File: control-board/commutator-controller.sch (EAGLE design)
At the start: 40 parts, among them U1 IS31FL3193, U2 LTC4425EMSE#PBF, U3 TEENSY_LC, U4 PTN04050C, U5 TMC2130

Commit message: Nearly complete control board
- Silkscreen still needs work: button labels, device label, etc
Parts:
- removed 1.2M, 1.5M: (no value), jonnew:R_0603
- removed IREF_AIN: (no value), jonnew:TP_2MM
- removed J2: (no value), jonnew:PINHD-1X4
- removed R17: 10k, jonnew:R_0402
- removed S4: (no value), jonnew:TOUCH_2X2CM
- removed TP1: RESET, jonnew:TP_1MM
- added GND1, GND2: (no value), jonnew:TPB2,54
- added J1: (no value), jonnew:PINHD-1X4_SMD-0.1"
- added R11: 500, jonnew:R_0603
- added R12, R13: 4.7k, jonnew:R_0603
- +3.3V, +5V, +5V1, GND: device jonnew:TP_2MM -> jonnew:TPB2,54
- C10: value 22uF -> 1F; device jonnew:C_1206 -> jonnew:C-POL_1210
- C2: value 10nF -> 22uF; device jonnew:C_0402 -> jonnew:C_1206
- C3: value 1uF/50V -> 22uF; device jonnew:C_0603 -> jonnew:C_1206
- C5: value 1F -> 100 uF; device jonnew:C-POL_1210 -> jonnew:C-POL_0807
- C6: value 2.2uF -> 100uF; device jonnew:C_0805 -> jonnew:C-POL_0807
- C7: value 100uF -> 2.2uF; device jonnew:C-POL_0807 -> jonnew:C_0805
- C8: value 100 uF -> 10nF; device jonnew:C-POL_0807 -> jonnew:C_0402
- C9: value 22uF -> 1uF; device jonnew:C_1206 -> jonnew:C_0603
- R1: device jonnew:R_0402 -> jonnew:R_0603
- R10, R9: value 4.7k -> 10k; device jonnew:R_0402 -> jonnew:R_0603
- R2: value 10k -> 1.5M
- R3: value 10k -> 1.33k
- R4: value 0 -> 1.2M
- R5: value DNP -> 0
- R6: value 10k -> DNP
- R7: value 1.33k -> 10k
- R8: value 500 -> 10k
- S1, S2: device jonnew:SPST_TACT_EVQP7 -> jonnew:TOUCH_2X2CM
- S3: device jonnew:TOUCH_2X2CM -> jonnew:SPST_TACT_EVQP7
- U1: value IS31FL3193 -> PTN04050C; device jonnew:IS31FL3193 -> jonnew:VREG_ADJ_R-PDSS-B4
- U3: value TEENSY_LC -> IS31FL3193; device jonnew:TEENSY_LC_SMD -> jonnew:IS31FL3193
- U4: value PTN04050C -> TMC2130; device jonnew:VREG_ADJ_R-PDSS-B4 -> jonnew:SILENT-STEPPER-STICK-TMC2130_SMD
- U5: value TMC2130 -> TEENSY_LC; device jonnew:SILENT-STEPPER-STICK-TMC2130_SMD -> jonnew:TEENSY_LC_SMD
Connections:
- removed net IREF: IREF_AIN.TP
- removed net N$23: S2.P, S2.P1, TP1.TP
- new net CFG-3/!TMC_CS: U4.CS/CFG3, U5.15/A1/T
- new net DIR: U4.DIR, U5.14/A0
- new net STEP: U4.STEP, U5.16/A2/T/PWM
- new net TMC_EN: U4.EN/CFG6, U5.17/A3/T/PWM
- net !IS31_SHDN: now also R8.1, U3.!SHDN, U5.2; no longer R17.1, U1.!SHDN
- net !PFO: now also R7.1, U5.23/A9/SDA1/T/PWM; no longer R6.1, U3.2
- net +3V3: now also R1.2, R12.1, R13.1, R7.2, U4.VIO, U5.3.3V0; no longer R6.2, U3.3.3V0
- net +5V0: now also C2.1, C5.+, R5.2, U1.VI; no longer C8.+, C9.1, R10.1, R4.2, R9.1, U4.VI
- net CCW: now also S2.1, U5.4/PWM; no longer S4.1, U3.1/TX1/T
- net CFG-0/MISO: now also U4.MISO/GFG0, U5.12/MISO; no longer U3.12/MISO
- net CFG-1/MOSI: now also U4.MOSI/GFG1, U5.11/MOSI; no longer U3.11/MOSI
- net CFG-2/SCLK: now also U4.SCLK/CFG2, U5.13/SCK0/LED; no longer U3.13/SCK0/LED
- net CHRG_CURR: now also R11.2, U5.21/A7; no longer R8.2
- net CW: now also S1.1, U5.0/RX1/T; no longer S3.1, U3.0/RX1/T
- net GND: now also C10.-, C6.-, C7.2, C8.2, GND1.TP, GND2.TP, R10.1, R11.1, R6.1, R8.2, R9.1, S3.S, S3.S1, U3.AD; no longer C10.2, C6.2, C7.-, C8.-, R17.2, R2.1, R5.1, R7.1, R8.1, S1.S1, S2.S, S2.S1, U1.AD
- net MOT_POW_EN: now also R10.2, U5.22/A8/SCL1/T/PWM; no longer R3.2, U3.3/PWM
- net N$1: now also R4.1; no longer 1.2M.1
- net N$10: now also U3.OUT2; no longer U1.OUT2
- net N$14: now also C10.+; no longer C5.+
- net N$2: now also R2.1, R4.2; no longer 1.2M.2, 1.5M.1
- net N$3: now also U3.OUT1; no longer U1.OUT1
- net N$4: now also R5.1, R6.2; no longer R4.1, R5.2
- net N$45: now also U3.OUT3; no longer U1.OUT3
- net N$5: now also J1.1, U4.M1B; no longer J2.1, U5.M1B
- net N$6: now also J1.2, U4.M1A; no longer J2.2, U5.M1A
- net N$7: now also J1.3, U4.M2A; no longer J2.3, U5.M2A
- net N$8: now also J1.4, U4.M2B; no longer J2.4, U5.M2B
- net N$9: now also R3.2, U1.ADJ; no longer R7.2, U4.ADJ
- net PROGRAM: now also S3.P, S3.P1, U5.PROGRAM; no longer S1.P, S1.P1, U3.PROGRAM
- net SCL: now also R13.2, U3.SCL, U5.19/A5/SCL0/T; no longer R10.2, U1.SCL, U3.19/A5/SCL0/T
- net SDA: now also R12.2, U3.SDA, U5.18/A4/SDA0/T; no longer R9.2, U1.SDA, U3.18/A4/SDA0/T
- net VCC: now also C7.1, C8.1, C9.1, R2.2, U3.VCC, U5.VIN; no longer 1.5M.2, C2.1, C3.1, C6.1, R1.2, U1.VCC, U3.VIN, U5.VIO
- net VMID_SEL: now also R9.2, U5.20/A6/SCK1/PWM; no longer R2.2, U3.4/PWM
- net VMOT: now also C3.1, C6.+, U1.VO, U4.VM; no longer C10.1, C7.+, U4.VO, U5.VM
- net V_BM: now also U3.V_BM, U5.3/PWM; no longer U1.V_BM
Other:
- note removed: "Teensy reset (jumper wire to reset pad on Teensy)"
- moved on the sheet: +3.3V, +5V, +5V1, C10, C2, C3, C5, C6, C7, C8, C9, GND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

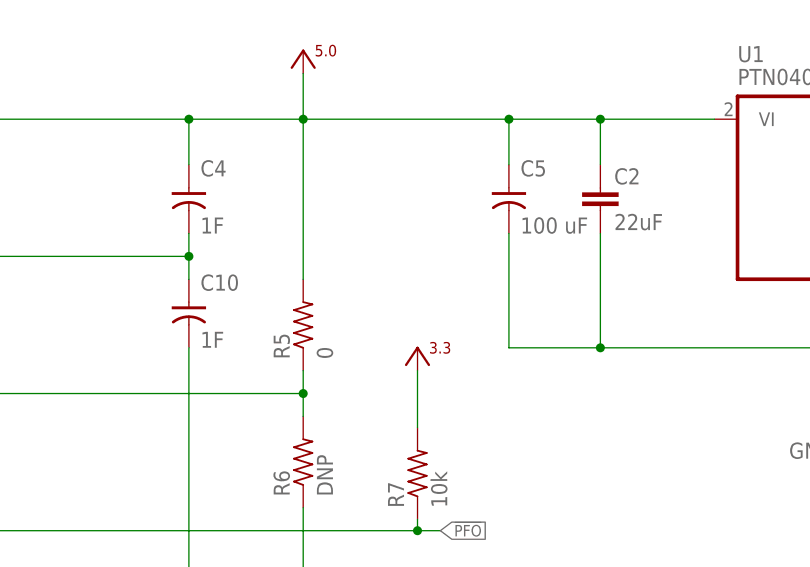
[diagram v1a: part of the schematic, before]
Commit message: Completed control board
- Pending review from jvoigts
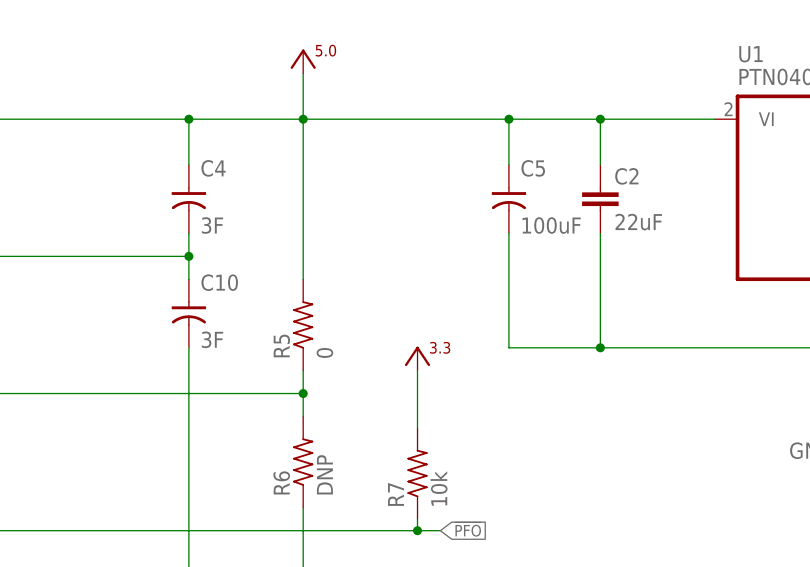
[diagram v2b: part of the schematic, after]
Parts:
- C10, C4: value 1F -> 3F
- C5: value 100 uF -> 100uF
- S1, S2: device jonnew:TOUCH_2X2CM -> jonnew:TOUCH_1MM
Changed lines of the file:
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@@
 <part name="U$2" library="jonnew" deviceset="VCC" device=""/>
 <part name="P+5" library="jonnew" deviceset="+5V" device=""/>
-<part name="C4" library="jonnew" deviceset="C-POL" device="_1210" value="1F"/>
-<part name="C10" library="jonnew" deviceset="C-POL" device="_1210" value="1F"/>
+<part name="C4" library="jonnew" deviceset="C-POL" device="_1210" value="3F"/>
+<part name="C10" library="jonnew" deviceset="C-POL" device="_1210" value="3F"/>
 <part name="SUPPLY2" library="jonnew" deviceset="GND" device=""/>
 <part name="SUPPLY3" library="jonnew" deviceset="GND" device=""/>
@@
 <part name="U$5" library="jonnew" deviceset="VCC" device=""/>
 <part name="SUPPLY18" library="jonnew" deviceset="+3V3" device=""/>
-<part name="S1" library="jonnew" deviceset="TOUCH" device="_2X2CM"/>
-<part name="S2" library="jonnew" deviceset="TOUCH" device="_2X2CM"/>
+<part name="S1" library="jonnew" deviceset="TOUCH" device="_1MM"/>
+<part name="S2" library="jonnew" deviceset="TOUCH" device="_1MM"/>
 <part name="S3" library="jonnew" deviceset="SPST_TACT" device="_EVQP7"/>
 <part name="+5V1" library="jonnew" deviceset="TP" device="B2,54"/>
@@
 <part name="SUPPLY7" library="jonnew" deviceset="GND" device=""/>
 <part name="C6" library="jonnew" deviceset="C-POL" device="_0807" value="100uF"/>
-<part name="C5" library="jonnew" deviceset="C-POL" device="_0807" value="100 uF"/>
+<part name="C5" library="jonnew" deviceset="C-POL" device="_0807" value="100uF"/>
 <part name="C2" library="jonnew" deviceset="C" device="_1206" value="22uF"/>
 <part name="C3" library="jonnew" deviceset="C" device="_1206" value="22uF"/>

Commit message: Added stop/go button to control board
- Added README
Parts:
- added S4: (no value), jonnew:TOUCH_1MM
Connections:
- new net STOP: S4.1, U5.17/A3/T/PWM
- net TMC_EN: now also U5.10/TX2/CS0/PWM; no longer U5.17/A3/T/PWM
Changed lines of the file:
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@@
 <part name="GND1" library="jonnew" deviceset="TP" device="B2,54"/>
 <part name="SUPPLY20" library="jonnew" deviceset="GND" device=""/>
+<part name="S4" library="jonnew" deviceset="TOUCH" device="_1MM"/>
 </parts>
 <sheets>
@@
 <instance part="GND1" gate="G$1" x="381" y="127"/>
 <instance part="SUPPLY20" gate="PE" x="381" y="116.84"/>
+<instance part="S4" gate="G$1" x="73.66" y="109.22"/>
 </instances>
 <busses>
@@
 </segment>
 <segment>
-<wire x1="96.52" y1="109.22" x2="86.36" y2="109.22" width="0.1524" layer="91"/>
-<label x="86.36" y="109.22" size="1.27" layer="95" rot="R180" xref="yes"/>
-<pinref part="U5" gate="G$1" pin="17/A3/T/PWM"/>
+<wire x1="96.52" y1="127" x2="86.36" y2="127" width="0.1524" layer="91"/>
+<label x="86.36" y="127" size="1.27" layer="95" rot="R180" xref="yes"/>
+<pinref part="U5" gate="G$1" pin="10/TX2/CS0/PWM"/>
 </segment>
 </net>
@@
 </segment>
 </net>
+<net name="STOP" class="0">
+<segment>
+<pinref part="S4" gate="G$1" pin="1"/>
+<pinref part="U5" gate="G$1" pin="17/A3/T/PWM"/>
+<wire x1="78.74" y1="109.22" x2="96.52" y2="109.22" width="0.1524" layer="91"/>
+</segment>
+</net>

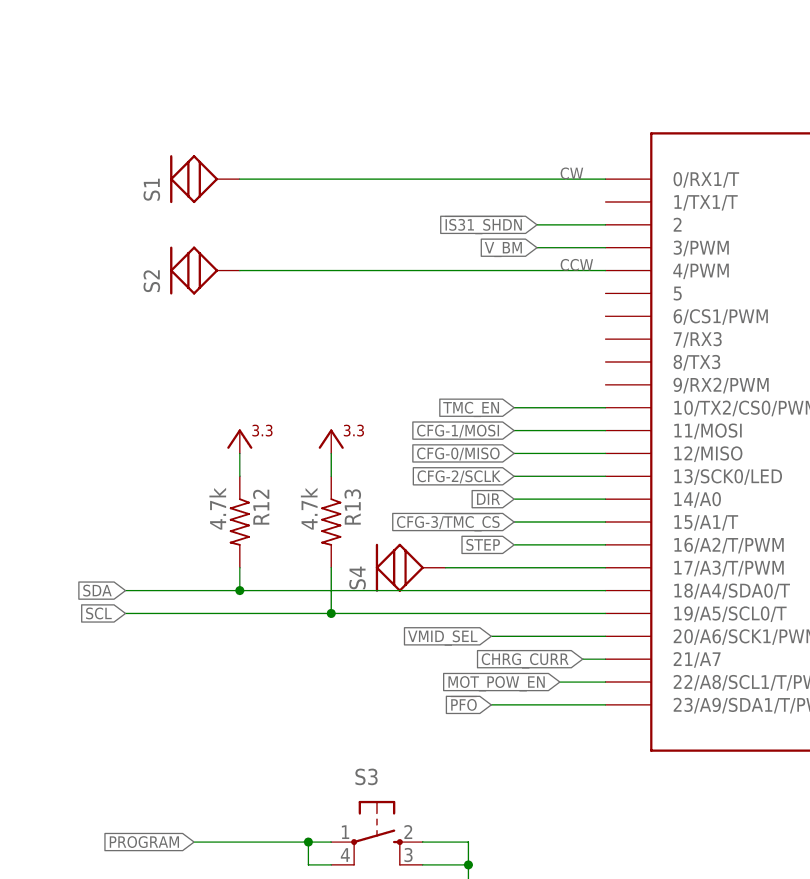
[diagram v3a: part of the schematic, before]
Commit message: Added fourth mode button on control board
- Sits around RGB LED window
- Also, increased min via drill size to 0.3mm which greatly decreases
board cost
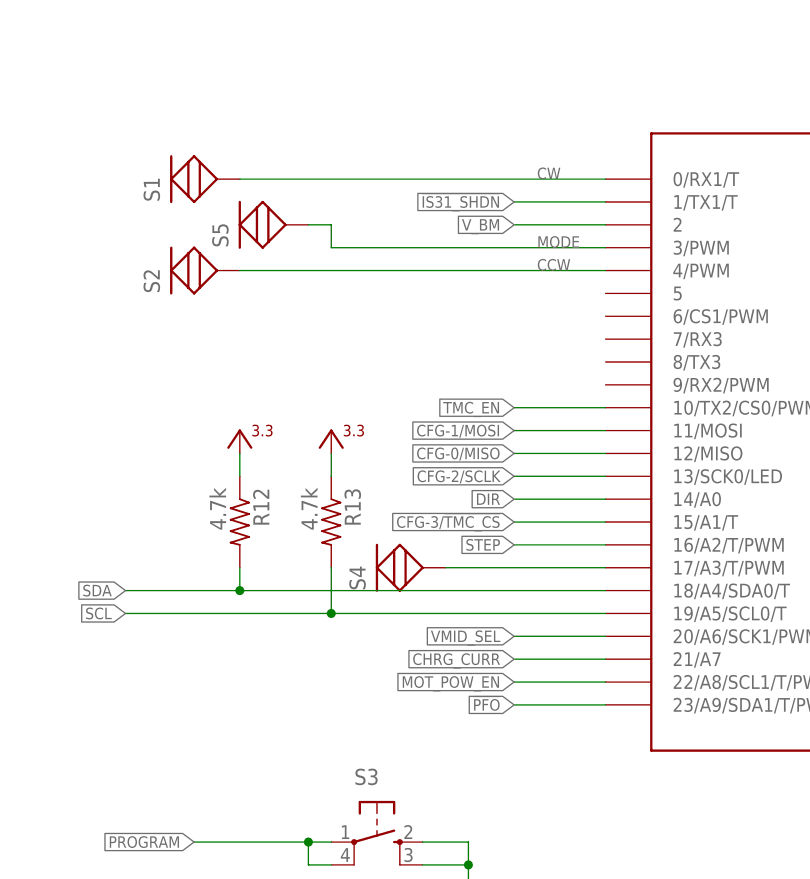
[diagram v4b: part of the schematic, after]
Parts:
- added S5: (no value), jonnew:TOUCH_1MM
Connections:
- new net MODE: S5.1, U5.3/PWM
- net !IS31_SHDN: now also U5.1/TX1/T; no longer U5.2
- net V_BM: now also U5.2; no longer U5.3/PWM
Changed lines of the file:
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@@
 <part name="SUPPLY20" library="jonnew" deviceset="GND" device=""/>
 <part name="S4" library="jonnew" deviceset="TOUCH" device="_1MM"/>
+<part name="S5" library="jonnew" deviceset="TOUCH" device="_1MM"/>
 </parts>
 <sheets>
@@
 <instance part="SUPPLY20" gate="PE" x="381" y="116.84"/>
 <instance part="S4" gate="G$1" x="73.66" y="109.22"/>
+<instance part="S5" gate="G$1" x="58.42" y="147.32"/>
 </instances>
 <busses>
@@
 </segment>
 <segment>
-<label x="88.9" y="144.78" size="1.27" layer="95" rot="R180" xref="yes"/>
-<wire x1="96.52" y1="144.78" x2="88.9" y2="144.78" width="0.1524" layer="91"/>
-<pinref part="U5" gate="G$1" pin="3/PWM"/>
+<label x="86.36" y="147.32" size="1.27" layer="95" rot="R180" xref="yes"/>
+<wire x1="96.52" y1="147.32" x2="86.36" y2="147.32" width="0.1524" layer="91"/>
+<pinref part="U5" gate="G$1" pin="2"/>
 </segment>
 </net>
@@
 </segment>
 <segment>
-<label x="88.9" y="147.32" size="1.27" layer="95" rot="R180" xref="yes"/>
-<wire x1="88.9" y1="147.32" x2="96.52" y2="147.32" width="0.1524" layer="91"/>
-<pinref part="U5" gate="G$1" pin="2"/>
+<label x="86.36" y="149.86" size="1.27" layer="95" rot="R180" xref="yes"/>
+<wire x1="86.36" y1="149.86" x2="96.52" y2="149.86" width="0.1524" layer="91"/>
+<pinref part="U5" gate="G$1" pin="1/TX1/T"/>
 </segment>
 </net>
@@
 </segment>
 <segment>
-<label x="83.82" y="101.6" size="1.27" layer="95" rot="R180" xref="yes"/>
-<wire x1="83.82" y1="101.6" x2="96.52" y2="101.6" width="0.1524" layer="91"/>
+<label x="86.36" y="101.6" size="1.27" layer="95" rot="R180" xref="yes"/>
+<wire x1="86.36" y1="101.6" x2="96.52" y2="101.6" width="0.1524" layer="91"/>
 <pinref part="U5" gate="G$1" pin="20/A6/SCK1/PWM"/>
 </segment>
@@
 </segment>
 <segment>
-<label x="91.44" y="96.52" size="1.27" layer="95" rot="R180" xref="yes"/>
-<wire x1="96.52" y1="96.52" x2="91.44" y2="96.52" width="0.1524" layer="91"/>
+<label x="86.36" y="96.52" size="1.27" layer="95" rot="R180" xref="yes"/>
+<wire x1="96.52" y1="96.52" x2="86.36" y2="96.52" width="0.1524" layer="91"/>
 <pinref part="U5" gate="G$1" pin="22/A8/SCL1/T/PWM"/>
 </segment>
@@
 </segment>
 <segment>
-<wire x1="96.52" y1="93.98" x2="83.82" y2="93.98" width="0.1524" layer="91"/>
-<label x="83.82" y="93.98" size="1.27" layer="95" rot="R180" xref="yes"/>
+<wire x1="96.52" y1="93.98" x2="86.36" y2="93.98" width="0.1524" layer="91"/>
+<label x="86.36" y="93.98" size="1.27" layer="95" rot="R180" xref="yes"/>
 <pinref part="U5" gate="G$1" pin="23/A9/SDA1/T/PWM"/>
 </segment>
@@
 </segment>
 <segment>
-<wire x1="96.52" y1="99.06" x2="93.98" y2="99.06" width="0.1524" layer="91"/>
-<label x="93.98" y="99.06" size="1.27" layer="95" rot="R180" xref="yes"/>
+<wire x1="96.52" y1="99.06" x2="86.36" y2="99.06" width="0.1524" layer="91"/>
+<label x="86.36" y="99.06" size="1.27" layer="95" rot="R180" xref="yes"/>
 <pinref part="U5" gate="G$1" pin="21/A7"/>
 </segment>
@@
 <pinref part="S1" gate="G$1" pin="1"/>
 <wire x1="96.52" y1="152.4" x2="55.88" y2="152.4" width="0.1524" layer="91"/>
-<label x="91.44" y="152.4" size="1.27" layer="95"/>
+<label x="88.9" y="152.4" size="1.27" layer="95"/>
 <pinref part="U5" gate="G$1" pin="0/RX1/T"/>
 </segment>
@@
 <wire x1="96.52" y1="142.24" x2="55.88" y2="142.24" width="0.1524" layer="91"/>
 <pinref part="S2" gate="G$1" pin="1"/>
-<label x="91.44" y="142.24" size="1.27" layer="95"/>
+<label x="88.9" y="142.24" size="1.27" layer="95"/>
 </segment>
 </net>
@@
 </segment>
 </net>
+<net name="MODE" class="0">
+<segment>
+<pinref part="S5" gate="G$1" pin="1"/>
+<wire x1="63.5" y1="147.32" x2="66.04" y2="147.32" width="0.1524" layer="91"/>
+<wire x1="66.04" y1="147.32" x2="66.04" y2="144.78" width="0.1524" layer="91"/>
+<pinref part="U5" gate="G$1" pin="3/PWM"/>
+<wire x1="66.04" y1="144.78" x2="96.52" y2="144.78" width="0.1524" layer="91"/>
+<label x="88.9" y="144.78" size="1.27" layer="95"/>
+</segment>
+</net>
